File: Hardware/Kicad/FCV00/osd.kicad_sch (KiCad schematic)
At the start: 14 parts, among them U9 AT7456E, Y2 27MHz 12pF

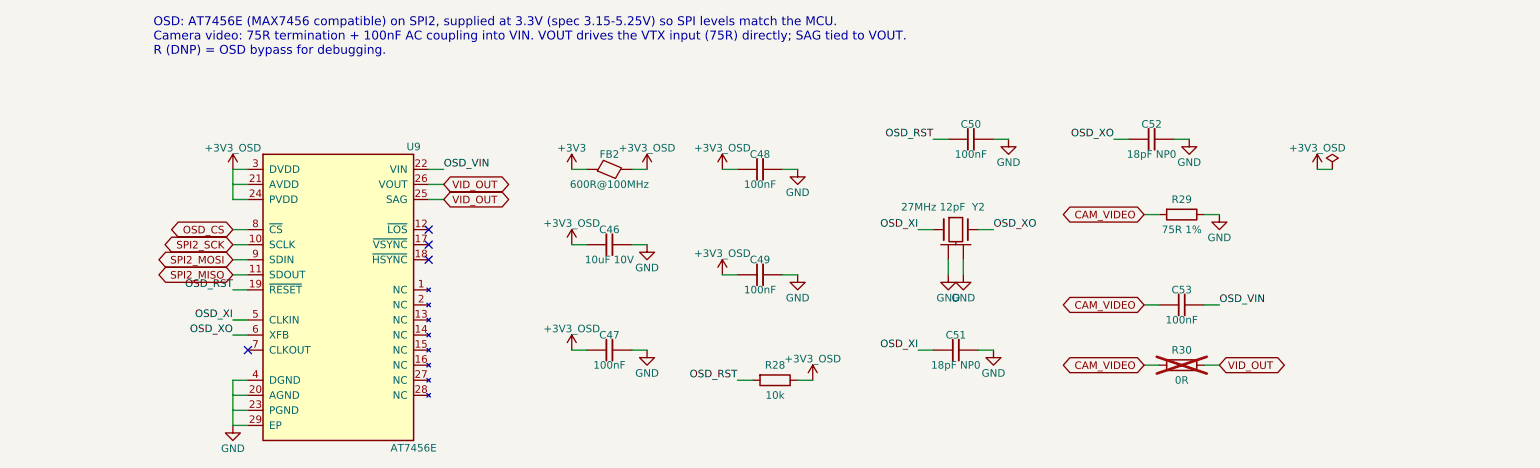
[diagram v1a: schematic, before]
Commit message: Boards follow the B0_EE part convention
- every real part uses the symbol/footprint/3D/datasheet named after its MPN in Kicad_Libs
- symbols keep only Reference, Value, Footprint, Datasheet, Description
  (MPN, Manufacturer, Verify, LCSC, Note fields removed; Verify notes moved to the Readme)
- schematic symbol caches rebuilt from the libraries, PCB footprints relinked with the
  same fields and 3D models as the library (connectivity unchanged)
- DNP and BOM attributes of the footprints match the symbols
- BOMs re-exported with kicad-cli
- ignore KiCad local history
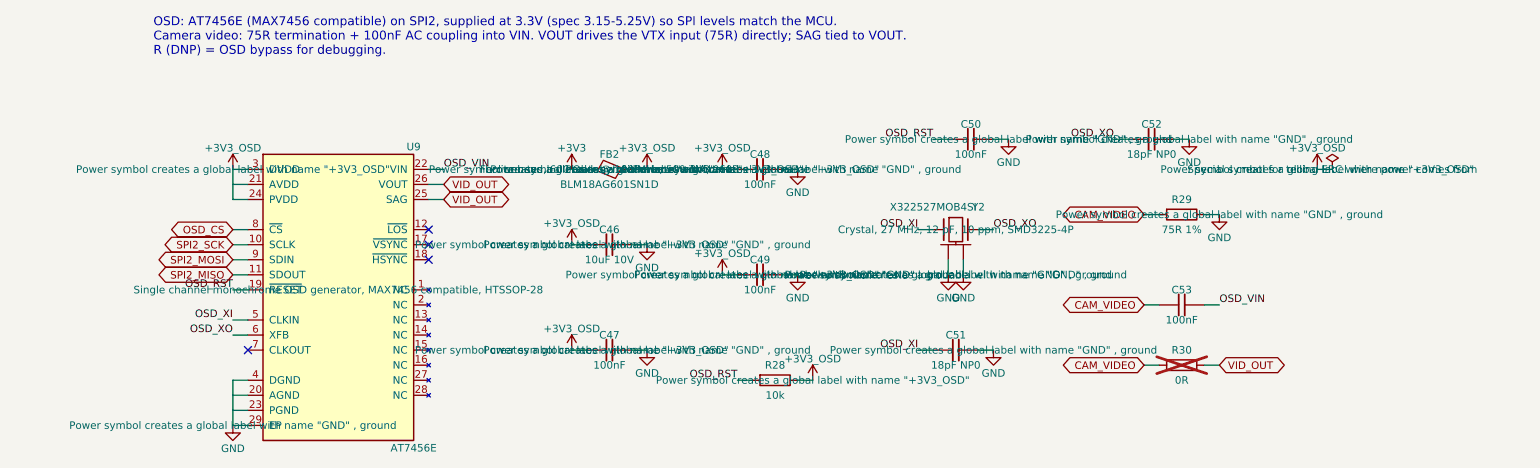
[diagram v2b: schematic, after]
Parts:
- FB2: value 600R@100MHz -> BLM18AG601SN1D; footprint eChoke:L_0603_1608Metric -> eFerrite:BLM18AG601SN1D; symbol eChoke:FB -> eFerrite:BLM18AG601SN1D; MPN BLM18AG601SN1D -> (none)
- U9: footprint eDisplay:HTSSOP-28-1EP_4.4x9.7mm_P0.65mm_EP2.85x5.4mm -> eDisplay:AT7456E; LCSC C82351 -> (none); MPN AT7456E -> (none); Manufacturer Shenzhen Zhongkewei (ZKW) -> (none); Verify Pin table = MAX7456 pinout (AT7456E is pin-compatible). Exp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 -> (none)
- Y2: value 27MHz 12pF -> X322527MOB4SI; footprint eCrystal:Crystal_SMD_3225-4Pin_3.2x2.5mm -> eCrystal:X322527MOB4SI; symbol eCrystal:Crystal_GND24 -> eCrystal:X322527MOB4SI; MPN X322527MOB4SI -> (none); Manufacturer Yangxing -> (none)
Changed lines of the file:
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@@
 			)
 		)
-		(property "Description" ""
+		(property "Description" "Power symbol creates a global label with name \"GND\" , ground"
 			(at 153.67 71.12 0)
 			(show_name no)
@@
 			)
 		)
-		(property "Description" ""
+		(property "Description" "Power symbol creates a global label with name \"+3V3_OSD\""
 			(at 95.25 40.64 0)
 			(show_name no)
@@
 			)
 		)
-		(property "Description" ""
+		(property "Description" "Power symbol creates a global label with name \"GND\" , ground"
 			(at 120.65 40.64 0)
 			(show_name no)
@@
 			)
 		)
-		(property "Description" ""
+		(property "Description" "Special symbol for telling ERC where power comes from"
 			(at 210.82 40.64 0)
 			(show_name no)
@@
 			)
 		)
-		(property "Description" ""
+		(property "Description" "Power symbol creates a global label with name \"GND\" , ground"
 			(at 95.25 53.34 0)
 			(show_name no)
@@
 	)
 	(symbol
-		(lib_id "eChoke:FB")
+		(lib_id "eFerrite:BLM18AG601SN1D")
 		(at 88.9 40.64 0)
 		(unit 1)
@@
 			)
 		)
-		(property "Value" "600R@100MHz"
+		(property "Value" "BLM18AG601SN1D"
 			(at 88.9 43.18 0)
 			(show_name no)
@@
 			)
 		)
-		(property "Footprint" "eChoke:L_0603_1608Metric"
+		(property "Footprint" "eFerrite:BLM18AG601SN1D"
 			(at 88.9 40.64 0)
 			(hide yes)
@@
 			)
 		)
-		(property "Datasheet" ""
+		(property "Datasheet" "${KIPRJMOD}/../KiCad_Libs/eFerrite/datasheet/BLM18AG601SN1D.pdf"
 			(at 88.9 40.64 0)
 			(hide yes)
@@
 			)
 		)
-		(property "Description" ""
+		(property "Description" "Ferrite bead, 600 Ohm @ 100 MHz, 500 mA, 0603"
 			(at 88.9 40.64 0)
-			(show_name no)
-			(do_not_autoplace no)
-			(effects
-				(font
-					(size 1.27 1.27)
-				)
-			)
-		)
-		(property "MPN" "BLM18AG601SN1D"
-			(at 88.9 40.64 0)
-			(hide yes)
 			(show_name no)
 			(do_not_autoplace no)
@@
 			)
 		)
-		(property "Description" ""
+		(property "Description" "Power symbol creates a global label with name \"+3V3_OSD\""
 			(at 107.95 58.42 0)
 			(show_name no)
@@
 			)
 		)
-		(property "Description" ""
+		(property "Description" "Power symbol creates a global label with name \"+3V3\""
 			(at 82.55 40.64 0)
 			(show_name no)
@@
 			)
 		)
-		(property "Description" ""
+		(property "Description" "Power symbol creates a global label with name \"GND\" , ground"
 			(at 25.4 83.82 0)
 			(show_name no)
@@
 			)
 		)
-		(property "Description" ""
+		(property "Description" "Power symbol creates a global label with name \"+3V3_OSD\""
 			(at 123.19 76.2 0)
 			(show_name no)
@@
 			)
 		)
-		(property "Description" ""
+		(property "Description" "Power symbol creates a global label with name \"+3V3_OSD\""
 			(at 82.55 53.34 0)
 			(show_name no)
@@
 			)
 		)
-		(property "Description" ""
+		(property "Description" "Power symbol creates a global label with name \"GND\" , ground"
 			(at 191.77 48.26 0)
 			(show_name no)
@@
 			)
 		)
-		(property "Footprint" "eDisplay:HTSSOP-28-1EP_4.4x9.7mm_P0.65mm_EP2.85x5.4mm"
+		(property "Footprint" "eDisplay:AT7456E"
 			(at 43.18 60.96 0)
 			(hide yes)
@@
 			)
 		)
-		(property "Datasheet" "https://www.lcsc.com/product-detail/C82351.html"
+		(property "Datasheet" "${KIPRJMOD}/../KiCad_Libs/eDisplay/datasheet/AT7456E.pdf"
 			(at 43.18 60.96 0)
 			(hide yes)
@@
 			)
 		)
-		(property "Description" ""
+		(property "Description" "Single channel monochrome OSD generator, MAX7456 compatible, HTSSOP-28"
 			(at 43.18 60.96 0)
 			(show_name no)
@@
 			)
 		)
-		(property "Manufacturer" "Shenzhen Zhongkewei (ZKW)"
-			(at 43.18 60.96 0)
-			(hide yes)
-			(show_name no)
-			(do_not_autoplace no)
-			(effects
-				(font
-					(size 1.27 1.27)
-				)
-			)
-		)
-		(property "MPN" "AT7456E"
-			(at 43.18 60.96 0)
-			(hide yes)
-			(show_name no)
-			(do_not_autoplace no)
-			(effects
-				(font
-					(size 1.27 1.27)
-				)
-			)
-		)
-		(property "LCSC" "C82351"
-			(at 43.18 60.96 0)
-			(hide yes)
-			(show_name no)
-			(do_not_autoplace no)
-			(effects
-				(font
-					(size 1.27 1.27)
-				)
-			)
-		)
-		(property "Verify" "Pin table = MAX7456 pinout (AT7456E is pin-compatible). Exposed-pad size of the footprint must be checked against the AT7456E package drawing."
-			(at 43.18 60.96 0)
-			(hide yes)
-			(show_name no)
-			(do_not_autoplace no)
-			(effects
-				(font
-					(size 1.27 1.27)
-				)
-			)
-		)
 		(pin "1"
 		)
@@
 	)
 	(symbol
-		(lib_id "eCrystal:Crystal_GND24")
+		(lib_id "eCrystal:X322527MOB4SI")
 		(at 147.32 50.8 0)
 		(unit 1)
@@
 			)
 		)
-		(property "Value" "27MHz 12pF"
+		(property "Value" "X322527MOB4SI"
 			(at 143.51 46.99 0)
 			(show_name no)
@@
 			)
 		)
-		(property "Footprint" "eCrystal:Crystal_SMD_3225-4Pin_3.2x2.5mm"
+		(property "Footprint" "eCrystal:X322527MOB4SI"
 			(at 147.32 50.8 0)
 			(hide yes)
@@
 			)
 		)
-		(property "Datasheet" ""
+		(property "Datasheet" "${KIPRJMOD}/../KiCad_Libs/eCrystal/datasheet/X322527MOB4SI.pdf"
 			(at 147.32 50.8 0)
 			(hide yes)
@@
 			)
 		)
-		(property "Description" ""
+		(property "Description" "Crystal, 27 MHz, 12 pF, 10 ppm, SMD3225-4P"
 			(at 147.32 50.8 0)
-			(show_name no)
-			(do_not_autoplace no)
-			(effects
-				(font
-					(size 1.27 1.27)
-				)
-			)
-		)
-		(property "MPN" "X322527MOB4SI"
-			(at 147.32 50.8 0)
-			(hide yes)
-			(show_name no)
-			(do_not_autoplace no)
-			(effects
-				(font
-					(size 1.27 1.27)
-				)
-			)
-		)
-		(property "Manufacturer" "Yangxing"
-			(at 147.32 50.8 0)
-			(hide yes)
 			(show_name no)
 			(do_not_autoplace no)
@@
 			)
 		)
-		(property "Description" ""
+		(property "Description" "Power symbol creates a global label with name \"GND\" , ground"
 			(at 120.65 58.42 0)
 			(show_name no)
@@
 			)
 		)
-		(property "Description" ""
+		(property "Description" "Power symbol creates a global label with name \"GND\" , ground"
 			(at 95.25 71.12 0)
 			(show_name no)
@@
 			)
 		)
-		(property "Description" ""
+		(property "Description" "Power symbol creates a global label with name \"GND\" , ground"
 			(at 146.05 58.42 0)
 			(show_name no)
@@
 			)
 		)
-		(property "Description" ""
+		(property "Description" "Power symbol creates a global label with name \"+3V3_OSD\""
 			(at 82.55 71.12 0)
 			(show_name no)
@@
 			)
 		)
-		(property "Description" ""
+		(property "Description" "Power symbol creates a global label with name \"+3V3_OSD\""
 			(at 208.28 40.64 0)
 			(show_name no)
@@
 			)
 		)
-		(property "Description" ""
+		(property "Description" "Power symbol creates a global label with name \"+3V3_OSD\""
 			(at 25.4 40.64 0)
 			(show_name no)
@@
 			)
 		)
-		(property "Description" ""
+		(property "Description" "Power symbol creates a global label with name \"GND\" , ground"
 			(at 148.59 58.42 0)
 			(show_name no)
@@
 			)
 		)
-		(property "Description" ""
+		(property "Description" "Power symbol creates a global label with name \"GND\" , ground"
 			(at 186.69 35.56 0)
 			(show_name no)
@@
 			)
 		)
-		(property "Description" ""
+		(property "Description" "Power symbol creates a global label with name \"GND\" , ground"
 			(at 156.21 35.56 0)
 			(show_name no)
@@
 			)
 		)
-		(property "Description" ""
+		(property "Description" "Power symbol creates a global label with name \"+3V3_OSD\""
 			(at 107.95 40.64 0)
 			(show_name no)

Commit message: Cleared all the descriptions and started Power section for FCV
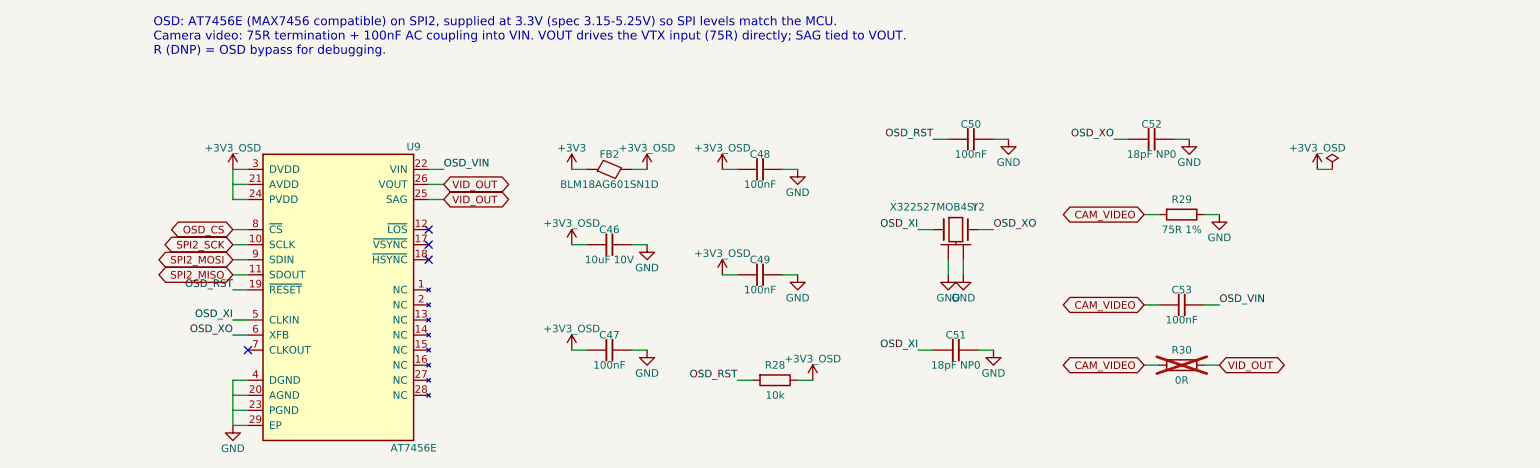
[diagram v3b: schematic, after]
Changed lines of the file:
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@@
 		(property "Description" "Power symbol creates a global label with name \"GND\" , ground"
 			(at 153.67 71.12 0)
+			(hide yes)
 			(show_name no)
 			(do_not_autoplace no)
@@
 		(property "Description" "Power symbol creates a global label with name \"+3V3_OSD\""
 			(at 95.25 40.64 0)
+			(hide yes)
 			(show_name no)
 			(do_not_autoplace no)
@@
 		(property "Description" "Power symbol creates a global label with name \"GND\" , ground"
 			(at 120.65 40.64 0)
+			(hide yes)
 			(show_name no)
 			(do_not_autoplace no)
@@
 		(property "Description" "Special symbol for telling ERC where power comes from"
 			(at 210.82 40.64 0)
+			(hide yes)
 			(show_name no)
 			(do_not_autoplace no)
@@
 		(property "Description" "Power symbol creates a global label with name \"GND\" , ground"
 			(at 95.25 53.34 0)
+			(hide yes)
 			(show_name no)
 			(do_not_autoplace no)
@@
 		(property "Description" "Ferrite bead, 600 Ohm @ 100 MHz, 500 mA, 0603"
 			(at 88.9 40.64 0)
+			(hide yes)
 			(show_name no)
 			(do_not_autoplace no)
@@
 		(property "Description" "Power symbol creates a global label with name \"+3V3_OSD\""
 			(at 107.95 58.42 0)
+			(hide yes)
 			(show_name no)
 			(do_not_autoplace no)
@@
 		(property "Description" "Power symbol creates a global label with name \"+3V3\""
 			(at 82.55 40.64 0)
+			(hide yes)
 			(show_name no)
 			(do_not_autoplace no)
@@
 		(property "Description" "Power symbol creates a global label with name \"GND\" , ground"
 			(at 25.4 83.82 0)
+			(hide yes)
 			(show_name no)
 			(do_not_autoplace no)
@@
 		(property "Description" "Power symbol creates a global label with name \"+3V3_OSD\""
 			(at 123.19 76.2 0)
+			(hide yes)
 			(show_name no)
 			(do_not_autoplace no)
@@
 		(property "Description" "Power symbol creates a global label with name \"+3V3_OSD\""
 			(at 82.55 53.34 0)
+			(hide yes)
 			(show_name no)
 			(do_not_autoplace no)
@@
 		(property "Description" "Power symbol creates a global label with name \"GND\" , ground"
 			(at 191.77 48.26 0)
+			(hide yes)
 			(show_name no)
 			(do_not_autoplace no)
@@
 		(property "Description" "Single channel monochrome OSD generator, MAX7456 compatible, HTSSOP-28"
 			(at 43.18 60.96 0)
+			(hide yes)
 			(show_name no)
 			(do_not_autoplace no)
@@
 		(property "Description" "Crystal, 27 MHz, 12 pF, 10 ppm, SMD3225-4P"
 			(at 147.32 50.8 0)
+			(hide yes)
 			(show_name no)
 			(do_not_autoplace no)
@@
 		(property "Description" "Power symbol creates a global label with name \"GND\" , ground"
 			(at 120.65 58.42 0)
+			(hide yes)
 			(show_name no)
 			(do_not_autoplace no)
@@
 		(property "Description" "Power symbol creates a global label with name \"GND\" , ground"
 			(at 95.25 71.12 0)
+			(hide yes)
 			(show_name no)
 			(do_not_autoplace no)
@@
 		(property "Description" "Power symbol creates a global label with name \"GND\" , ground"
 			(at 146.05 58.42 0)
+			(hide yes)
 			(show_name no)
 			(do_not_autoplace no)
@@
 		(property "Description" "Power symbol creates a global label with name \"+3V3_OSD\""
 			(at 82.55 71.12 0)
+			(hide yes)
 			(show_name no)
 			(do_not_autoplace no)
@@
 		(property "Description" "Power symbol creates a global label with name \"+3V3_OSD\""
 			(at 208.28 40.64 0)
+			(hide yes)
 			(show_name no)
 			(do_not_autoplace no)
@@
 		(property "Description" "Power symbol creates a global label with name \"+3V3_OSD\""
 			(at 25.4 40.64 0)
+			(hide yes)
 			(show_name no)
 			(do_not_autoplace no)
@@
 		(property "Description" "Power symbol creates a global label with name \"GND\" , ground"
 			(at 148.59 58.42 0)
+			(hide yes)
 			(show_name no)
 			(do_not_autoplace no)
@@
 		(property "Description" "Power symbol creates a global label with name \"GND\" , ground"
 			(at 186.69 35.56 0)
+			(hide yes)
 			(show_name no)
 			(do_not_autoplace no)
@@
 		(property "Description" "Power symbol creates a global label with name \"GND\" , ground"
 			(at 156.21 35.56 0)
+			(hide yes)
 			(show_name no)
 			(do_not_autoplace no)
@@
 		(property "Description" "Power symbol creates a global label with name \"+3V3_OSD\""
 			(at 107.95 40.64 0)
-			(show_name no)
-			(do_not_autoplace no)
+			(hide yes)
+			(show_name no)
+			(do_not_autoplace no)
